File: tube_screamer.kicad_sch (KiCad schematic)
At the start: 38 parts, among them Q1 BC817, U1 TL072

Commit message: PCB layout.
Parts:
- U1: footprint Package_SO:SOIC-8-1EP_3.9x4.9mm_P1.27mm_EP2.514x3.2mm -> Package_SO:SOIC-8_3.9x4.9mm_P1.27mm
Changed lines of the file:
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@@
 	(wire
 		(pts
-			(xy 85.725 178.435) (xy 85.725 179.07)
+			(xy 92.71 184.15) (xy 92.71 185.42)
 		)
 		(stroke
@@
 	(wire
 		(pts
+			(xy 85.725 184.15) (xy 85.725 178.435)
+		)
+		(stroke
+			(width 0)
+			(type default)
+		)
+	)
+	(wire
+		(pts
 			(xy 80.01 65.405) (xy 81.915 65.405)
 		)
@@
 	(wire
 		(pts
+			(xy 92.71 184.15) (xy 85.725 184.15)
+		)
+		(stroke
+			(width 0)
+			(type default)
+		)
+	)
+	(wire
+		(pts
 			(xy 121.92 80.01) (xy 121.285 80.01)
 		)
@@
 			)
 		)
-		(property "Footprint" "Package_SO:SOIC-8-1EP_3.9x4.9mm_P1.27mm_EP2.514x3.2mm"
+		(property "Footprint" "Package_SO:SOIC-8_3.9x4.9mm_P1.27mm"
 			(at 129.54 82.55 0)
 			(effects
@@
 			)
 		)
-		(property "Footprint" "Package_SO:SOIC-8-1EP_3.9x4.9mm_P1.27mm_EP2.514x3.2mm"
+		(property "Footprint" "Package_SO:SOIC-8_3.9x4.9mm_P1.27mm"
 			(at 104.775 161.29 0)
 			(effects
@@
 	(symbol
 		(lib_id "Simulation_SPICE:0")
-		(at 85.725 179.07 0)
+		(at 92.71 185.42 0)
 		(unit 1)
 		(exclude_from_sim no)
@@
 		(fields_autoplaced yes)
 		(property "Reference" "#GND04"
-			(at 85.725 181.61 0)
+			(at 92.71 187.96 0)
 			(effects
 				(font
@@
 		)
 		(property "Value" "0"
-			(at 85.725 177.165 0)
+			(at 92.71 183.515 0)
 			(effects
 				(font
@@
 		)
 		(property "Footprint" ""
-			(at 85.725 179.07 0)
+			(at 92.71 185.42 0)
 			(effects
 				(font
@@
 		)
 		(property "Datasheet" "~"
-			(at 85.725 179.07 0)
+			(at 92.71 185.42 0)
 			(effects
 				(font
@@
 		)
 		(property "Description" ""
-			(at 85.725 179.07 0)
+			(at 92.71 185.42 0)
 			(effects
 				(font
@@
 			)
 		)
-		(property "Footprint" "Package_SO:SOIC-8-1EP_3.9x4.9mm_P1.27mm_EP2.514x3.2mm"
+		(property "Footprint" "Package_SO:SOIC-8_3.9x4.9mm_P1.27mm"
 			(at 186.055 85.09 0)
 			(effects

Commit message: PCB update.
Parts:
- added TP10: ground, TestPoint:TestPoint_Pad_2.0x2.0mm, symbol Connector:TestPoint
- added TP9: input, TestPoint:TestPoint_Pad_2.0x2.0mm, symbol Connector:TestPoint
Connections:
- net 0: now also TP10.1
- net at R7.2: now also TP9.1
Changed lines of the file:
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@@
+	(wire
+		(pts
+			(xy 226.06 85.09) (xy 223.52 85.09)
+		)
+		(stroke
+			(width 0)
+			(type default)
+		)
+	)
 	(wire
 		(pts
@@
 	(wire
 		(pts
+			(xy 228.6 101.6) (xy 228.6 95.25)
+		)
+		(stroke
+			(width 0)
+			(type default)
+		)
+	)
+	(wire
+		(pts
+			(xy 228.6 95.25) (xy 220.98 95.25)
+		)
+		(stroke
+			(width 0)
+			(type default)
+		)
+	)
+	(wire
+		(pts
 			(xy 22.86 85.09) (xy 22.86 87.63)
 		)
@@
 		(pts
 			(xy 134.62 73.025) (xy 137.16 73.025)
+		)
+		(stroke
+			(width 0)
+			(type default)
+		)
+	)
+	(wire
+		(pts
+			(xy 226.06 82.55) (xy 226.06 85.09)
 		)
 		(stroke
@@
 	)
 	(symbol
+		(lib_id "Simulation_SPICE:0")
+		(at 228.6 101.6 0)
+		(unit 1)
+		(exclude_from_sim no)
+		(in_bom yes)
+		(on_board yes)
+		(dnp no)
+		(fields_autoplaced yes)
+		(property "Reference" "#GND07"
+			(at 228.6 104.14 0)
+			(effects
+				(font
+					(size 1.27 1.27)
+				)
+				(hide yes)
+			)
+		)
+		(property "Value" "0"
+			(at 228.6 99.695 0)
+			(effects
+				(font
+					(size 1.27 1.27)
+				)
+			)
+		)
+		(property "Footprint" ""
+			(at 228.6 101.6 0)
+			(effects
+				(font
+					(size 1.27 1.27)
+				)
+				(hide yes)
+			)
+		)
+		(property "Datasheet" "~"
+			(at 228.6 101.6 0)
+			(effects
+				(font
+					(size 1.27 1.27)
+				)
+				(hide yes)
+			)
+		)
+		(property "Description" ""
+			(at 228.6 101.6 0)
+			(effects
+				(font
+					(size 1.27 1.27)
+				)
+			)
+		)
+		(pin "1"
+		)
+		(instances
+			(project "tube_screamer"
+				(path "/e0801131-6974-42d8-8070-4ed960891aa7"
+					(reference "#GND07")
+					(unit 1)
+				)
+			)
+		)
+	)
+	(symbol
 		(lib_id "Device:R")
 		(at 117.475 92.71 0)
@@
 	(symbol
 		(lib_id "Connector:TestPoint")
+		(at 226.06 82.55 0)
+		(unit 1)
+		(exclude_from_sim no)
+		(in_bom yes)
+		(on_board yes)
+		(dnp no)
+		(fields_autoplaced yes)
+		(property "Reference" "TP9"
+			(at 227.965 77.978 0)
+			(effects
+				(font
+					(size 1.27 1.27)
+				)
+				(justify left)
+			)
+		)
+		(property "Value" "input"
+			(at 227.965 80.518 0)
+			(effects
+				(font
+					(size 1.27 1.27)
+				)
+				(justify left)
+			)
+		)
+		(property "Footprint" "TestPoint:TestPoint_Pad_2.0x2.0mm"
+			(at 231.14 82.55 0)
+			(effects
+				(font
+					(size 1.27 1.27)
+				)
+				(hide yes)
+			)
+		)
+		(property "Datasheet" "~"
+			(at 231.14 82.55 0)
+			(effects
+				(font
+					(size 1.27 1.27)
+				)
+				(hide yes)
+			)
+		)
+		(property "Description" ""
+			(at 226.06 82.55 0)
+			(effects
+				(font
+					(size 1.27 1.27)
+				)
+			)
+		)
+		(pin "1"
+		)
+		(instances
+			(project "tube_screamer"
+				(path "/e0801131-6974-42d8-8070-4ed960891aa7"
+					(reference "TP9")
+					(unit 1)
+				)
+			)
+		)
+	)
+	(symbol
+		(lib_id "Connector:TestPoint")
 		(at 86.995 160.02 270)
 		(unit 1)
@@
 					(unit 1)
 				)
+			)
+		)
+	)
+	(symbol
+		(lib_id "Connector:TestPoint")
+		(at 220.98 95.25 90)
+		(unit 1)
+		(exclude_from_sim yes)
+		(in_bom yes)
+		(on_board yes)
+		(dnp no)
+		(property "Reference" "TP10"
+			(at 213.995 88.9 90)
+			(effects
+				(font
+					(size 1.27 1.27)
+				)
+			)
+		)
+		(property "Value" "ground"
+			(at 213.995 91.44 90)
+			(effects
+				(font
+					(size 1.27 1.27)
+				)
+			)
+		)
+		(property "Footprint" "TestPoint:TestPoint_Pad_2.0x2.0mm"
+			(at 220.98 90.17 0)
+			(effects
+				(font
+					(size 1.27 1.27)
+				)
+				(hide yes)
+			)
+		)
+		(property "Datasheet" "~"
+			(at 220.98 90.17 0)
+			(effects
+				(font
+					(size 1.27 1.27)
+				)
+				(hide yes)
+			)
+		)
+		(property "Description" ""
+			(at 220.98 95.25 0)
+			(effects
+				(font
+					(size 1.27 1.27)
+				)
+			)
+		)
+		(pin "1"
+		)
+		(instances
+			(project "tube_screamer"
+				(path "/e0801131-6974-42d8-8070-4ed960891aa7"
+					(reference "TP10")
+					(unit 1)
+				)

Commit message: Updated schematic
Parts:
- removed C8: 10u, Capacitor_SMD:C_0603_1608Metric_Pad1.08x0.95mm_HandSolder, symbol Device:C
- removed D4: 1N4148WS, Diode_SMD:D_SOD-323, symbol Diode:1N4148WS
- removed R10, R9: 47k, Resistor_SMD:R_0603_1608Metric_Pad0.98x0.95mm_HandSolder, symbol Device:R
- removed R5: 4.7k, Resistor_SMD:R_0603_1608Metric_Pad0.98x0.95mm_HandSolder, symbol Device:R
- removed R8: 510, Resistor_SMD:R_0603_1608Metric_Pad0.98x0.95mm_HandSolder, symbol Device:R
- removed TP3: Red Error LED, TestPoint:TestPoint_Pad_2.0x2.0mm, symbol Connector:TestPoint
- removed TP4, TP6: ground, TestPoint:TestPoint_Pad_2.0x2.0mm, symbol Connector:TestPoint
- removed TP5: Power Supply, TestPoint:TestPoint_Pad_2.0x2.0mm, symbol Connector:TestPoint
- removed V2: 9, symbol Simulation_SPICE:VDC
- removed V3: VSIN, symbol Simulation_SPICE:VSIN
- added C11, C13, C14: 10u, Capacitor_SMD:C_0603_1608Metric_Pad1.08x0.95mm_HandSolder, symbol Device:C
- added C12: 100n, Capacitor_SMD:C_0603_1608Metric_Pad1.08x0.95mm_HandSolder, symbol Device:C
- added Q2, Q3: MMBT5551, Package_TO_SOT_SMD:SOT-23, symbol Transistor_BJT:BC817
- added R14, R16, R18: 1k, Resistor_SMD:R_0603_1608Metric_Pad0.98x0.95mm_HandSolder, symbol Device:R
- added R19: 510k, Resistor_SMD:R_0603_1608Metric_Pad0.98x0.95mm_HandSolder, symbol Device:R
- added R20, R21, R22, R23: 10k, Resistor_SMD:R_0603_1608Metric_Pad0.98x0.95mm_HandSolder, symbol Device:R
- added RV2: 20k, Potentiometer_THT:Potentiometer_Alpha_RD901F-40-00D_Single_Vertical, symbol Device:R_Potentiometer
- added RV3: 100k, Potentiometer_THT:Potentiometer_Alpha_RD901F-40-00D_Single_Vertical, symbol Device:R_Potentiometer
- added TP11: input, TestPoint:TestPoint_Pad_2.0x2.0mm, symbol Connector:TestPoint
- added TP12: ground, TestPoint:TestPoint_Pad_2.0x2.0mm, symbol Connector:TestPoint
- C1: LCSC (none) -> C1622
- C10: LCSC (none) -> C15849
- C3: value 51p -> 47p; LCSC (none) -> C1671
- C4: LCSC (none) -> C21120
- C5: LCSC (none) -> C14663
- C6: value 220p -> 220n; LCSC (none) -> C21120
- C7: value 220n -> 1u; LCSC (none) -> C15849
- C9: LCSC (none) -> C21122
- D1, D2, D3: LCSC (none) -> C2128
- Q1: value BC817 -> MMBT5551; LCSC (none) -> C2145
- R11: value 25k -> 100; footprint Resistor_SMD:R_0402_1005Metric -> Resistor_SMD:R_0603_1608Metric_Pad0.98x0.95mm_HandSolder; LCSC (none) -> C22775; now fitted; now in the parts list
- R12: value 1000k -> 1 Meg; LCSC (none) -> C22935
- R13: LCSC (none) -> C21190
- R15: value 470k -> 510k; LCSC (none) -> C23192
- R17, R3: LCSC (none) -> C25804
- R2: LCSC (none) -> C23162
- R4: value 10k -> 1k; LCSC (none) -> C21190
- R6: value 680k -> 1k; LCSC (none) -> C21190
- R7: value 1k -> 220; LCSC (none) -> C25804
- TP9: value input -> output
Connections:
- net 0: now also C4.1, R7.2, C13.2, C14.2, R20.2, R21.2, R23.2, RV3.3, TP12.1
- net 4V5: now also C14.1, R19.1, R22.2, R23.1
- net 9V: now also Q2.3 (C), Q3.2 (E), R22.1
- net at C3.2, D1.2 (A), D2.1 (K)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: now also R4.2, RV1.1; no longer C4.1
- net at C7.2: now also R14.2; no longer R7.1
- net at TP9.1: now also C11.2, R21.1; no longer R7.2
- net at C5.2, U1.6 (-): now also R6.2, RV2.3; no longer C6.1, R6.1
- net at C7.1, U1.7: now also R6.1; no longer C6.2, R6.2
- net at D3.2 (A): now also TP11.1
- net at C4.2, R4.1: now also C5.1, RV2.1
- net at R11.2: now also C11.1
- net at R12.1, R13.2, TP7.1: no longer R11.1
- new net: C13.1, Q3.1 (B), R16.1
- new net: D3.1 (K), Q3.3 (C), R16.2
- new net: C12.2, Q2.1 (B), R19.2
- new net: Q2.2 (E), R11.1, R20.1
- new net: R14.1, RV3.1
- new net: R18.2, RV3.2
- new net: C12.1, R18.1
- new net: C6.1, RV2.2
- new net: C6.2, R7.1
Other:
- moved on the sheet: C1, C10, C3, C5, C9, D1, Q1, R12, R13, R15, R17, R2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

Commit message: Updated schematic and layout.
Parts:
- TP10, TP11, TP12, TP7, TP8, TP9: footprint TestPoint:TestPoint_Pad_2.0x2.0mm -> TestPoint:TestPoint_THTPad_2.5x2.5mm_Drill1.2mm
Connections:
- net 0: now also RV3.1; no longer RV3.3
- net at C3.1, D1.1 (K), D2.2 (A)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: now also RV1.1; no longer RV1.3
- net at C3.2, D1.2 (A), D2.1 (K)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: now also RV1.3; no longer RV1.1
- net at R14.1: now also RV3.3; no longer RV3.1
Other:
- moved on the sheet: RV1
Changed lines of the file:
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@@
 			)
 		)
-		(property "Footprint" "TestPoint:TestPoint_Pad_2.0x2.0mm"
+		(property "Footprint" "TestPoint:TestPoint_THTPad_2.5x2.5mm_Drill1.2mm"
 			(at 34.29 90.17 0)
 			(effects
@@
 		(lib_id "Device:R_Potentiometer")
 		(at 193.04 69.85 0)
+		(mirror x)
 		(unit 1)
 		(exclude_from_sim no)
@@
 		(on_board yes)
 		(dnp no)
-		(fields_autoplaced yes)
 		(property "Reference" "RV3"
-			(at 190.5 68.5799 0)
+			(at 190.5 71.1201 0)
 			(effects
 				(font
@@
 		)
 		(property "Value" "100k"
-			(at 190.5 71.1199 0)
+			(at 190.5 68.5801 0)
 			(effects
 				(font
@@
 			)
 		)
-		(property "Footprint" "TestPoint:TestPoint_Pad_2.0x2.0mm"
+		(property "Footprint" "TestPoint:TestPoint_THTPad_2.5x2.5mm_Drill1.2mm"
 			(at 274.32 73.66 0)
 			(effects
@@
 			)
 		)
-		(property "Footprint" "TestPoint:TestPoint_Pad_2.0x2.0mm"
+		(property "Footprint" "TestPoint:TestPoint_THTPad_2.5x2.5mm_Drill1.2mm"
 			(at 29.21 153.67 0)
 			(effects
@@
 			)
 		)
-		(property "Footprint" "TestPoint:TestPoint_Pad_2.0x2.0mm"
+		(property "Footprint" "TestPoint:TestPoint_THTPad_2.5x2.5mm_Drill1.2mm"
 			(at 274.32 105.41 0)
 			(effects
@@
 	(symbol
 		(lib_id "Device:R_Potentiometer")
-		(at 110.49 29.21 270)
+		(at 110.49 29.21 90)
+		(mirror x)
 		(unit 1)
 		(exclude_from_sim no)
@@
 		(on_board yes)
 		(dnp no)
-		(fields_autoplaced yes)
 		(property "Reference" "RV1"
 			(at 110.49 22.86 90)
@@
 			)
 		)
-		(property "Footprint" "TestPoint:TestPoint_Pad_2.0x2.0mm"
+		(property "Footprint" "TestPoint:TestPoint_THTPad_2.5x2.5mm_Drill1.2mm"
 			(at 30.48 177.8 0)
 			(effects
@@
 			)
 		)
-		(property "Footprint" "TestPoint:TestPoint_Pad_2.0x2.0mm"
+		(property "Footprint" "TestPoint:TestPoint_THTPad_2.5x2.5mm_Drill1.2mm"
 			(at 34.29 54.61 0)
 			(effects

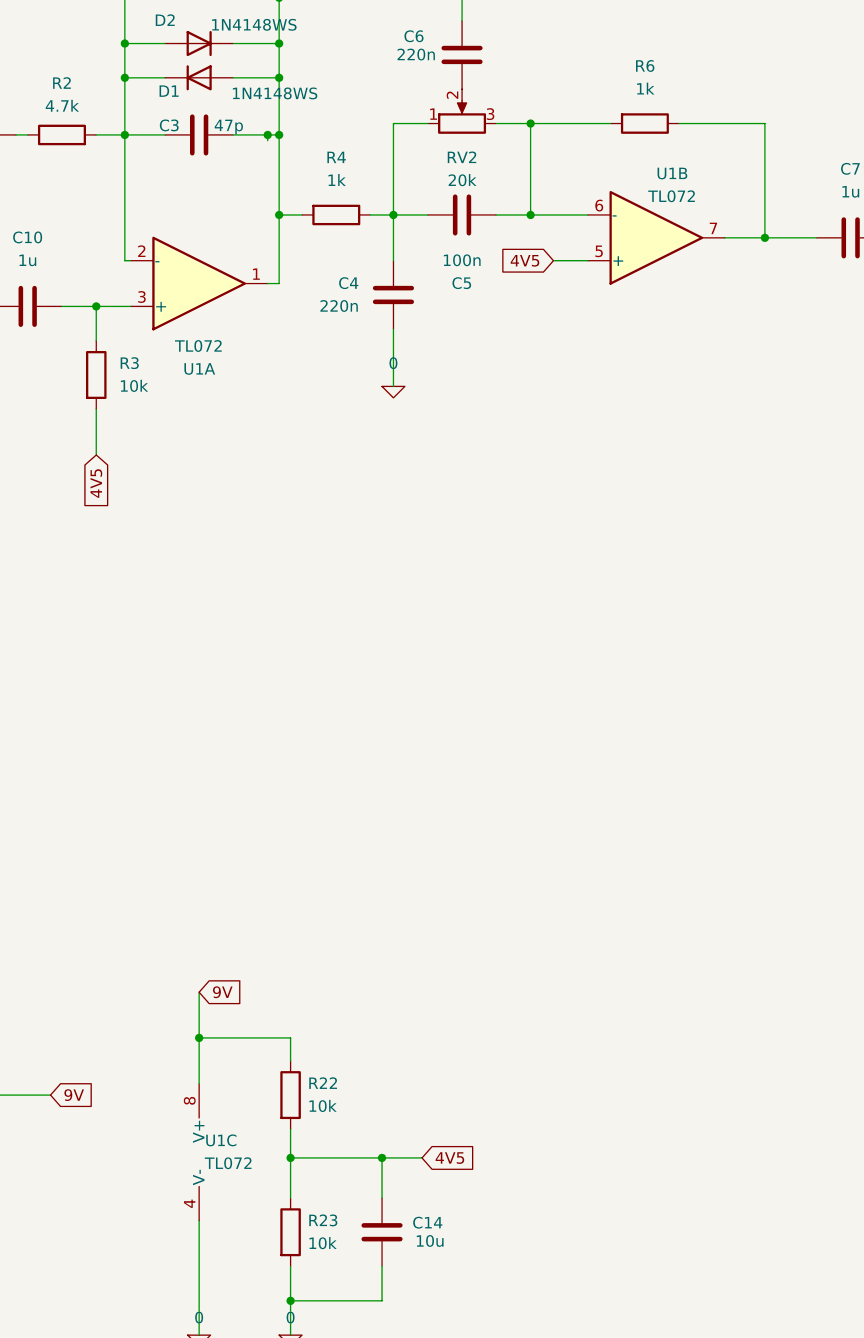
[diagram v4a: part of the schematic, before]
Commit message: Changed opamp to NE5532, basic LCSC part.
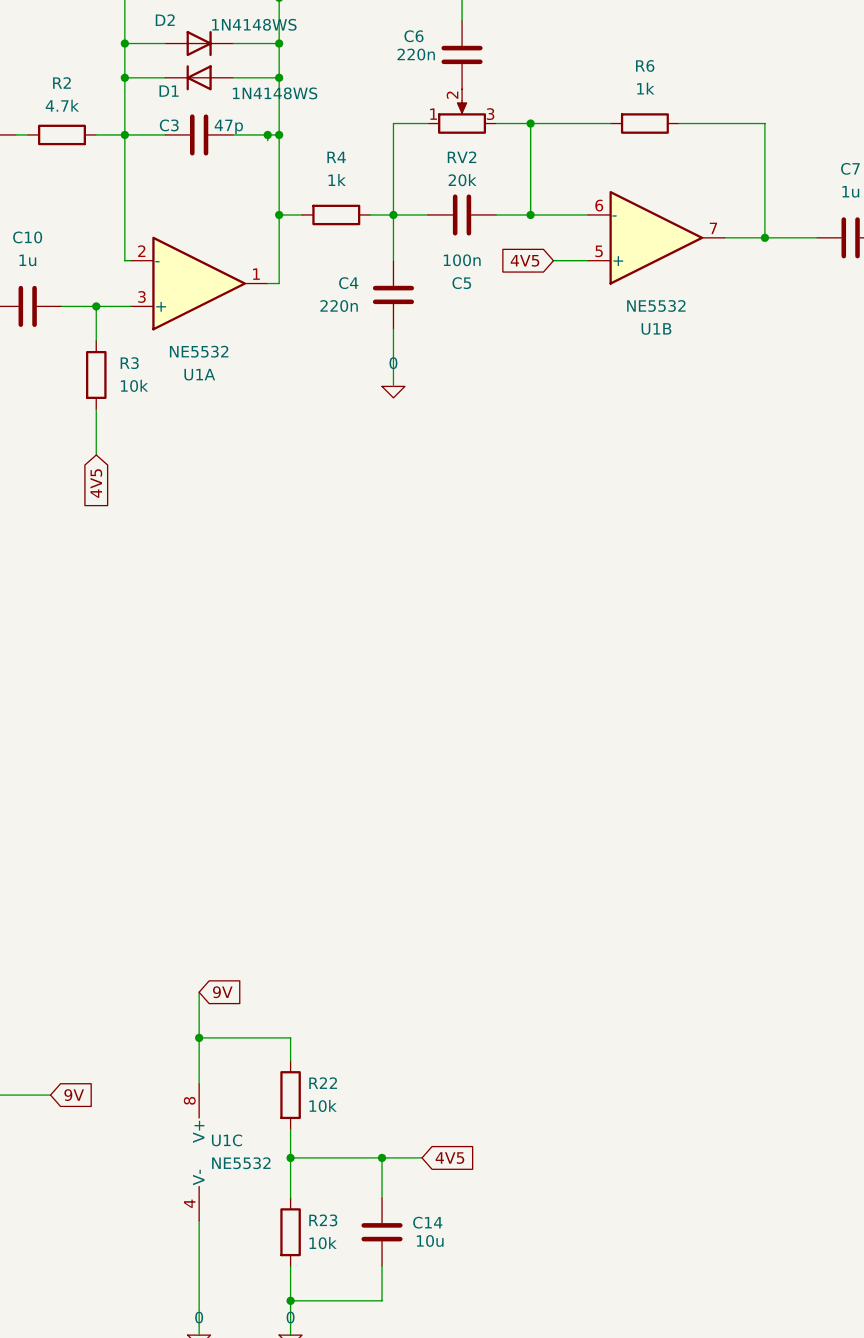
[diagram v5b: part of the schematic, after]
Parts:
- removed U1: TL072, Package_SO:SOIC-8_3.9x4.9mm_P1.27mm, symbol SPICE_opamps:TL072
- added U1: NE5532, Package_SO:SOIC-8_3.9x4.9mm_P1.27mm, symbol Amplifier_Operational:NE5532
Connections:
- net 0: now also U1.4 (V-)
- net 4V5: now also U1.5 (+)
- net 9V: now also U1.8 (V+)
- net at C3.1, D1.1 (K), D2.2 (A)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: now also U1.2 (-)
- net at C3.2, D1.2 (A), D2.1 (K)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: now also U1.1
- net at C7.1, R6.1: now also U1.7
- net at C5.2, R6.2, RV2.3: now also U1.6 (-)
- net at C10.2, R3.1: now also U1.3 (+)
